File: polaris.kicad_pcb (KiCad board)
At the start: 4 copper layers, 75 x 155 mm, 163 parts, among them J1001 Conn_Coaxial, J101 XT60-M, J102 SPI, J103 I2C, J104 PB, J105 SWD, J106 PYRO5, J107 PYRO4, J108 PYRO3, J109 PYRO2, J110 PYRO1, J111 PYRO0, J112 SERVO0, J113 SERVO1, J114 SERVO2, J115 SERVO3, J116 SERVO4, J117 SERVO5, J301 USB_C_Receptacle_USB2.0_16P, J401 GNSS, J501 XT60-M, Q201 IRLZ44N, Q202 IRLZ44N, Q401 Q_NMOS, Q501 IRLZ44N, Q502 IRLZ44N, Q503 IRLZ44N, Q504 IRLZ44N, Q505 IRLZ44N, Q506 IRLZ44N, SW401 SW_Push, SW402 SW_Push, U1001 Ra-08H, U1101 THD-2528-11SD-GF, U1201 W25Q128JVE, U201 BQ24005, U202 LM74700, U203 LM74700, U204 TLV75733PDBV, U205 LMR51430, U206 TPS7A2033PDBVR, U301 USBLC6-2SC6, U302 CH224K, U303 USBLC6-2SC6, U401 STM32F446VETx, U501 PC817, U502 PC817, U503 CD4051B, U504 PC817, U505 PC817, U506 PC817, U507 PC817, U601 ICM-42688-P, U701 LSM6DSO32TR, U801 MS5607, U901 LPS22HH, Y401 YXC YSX321SL

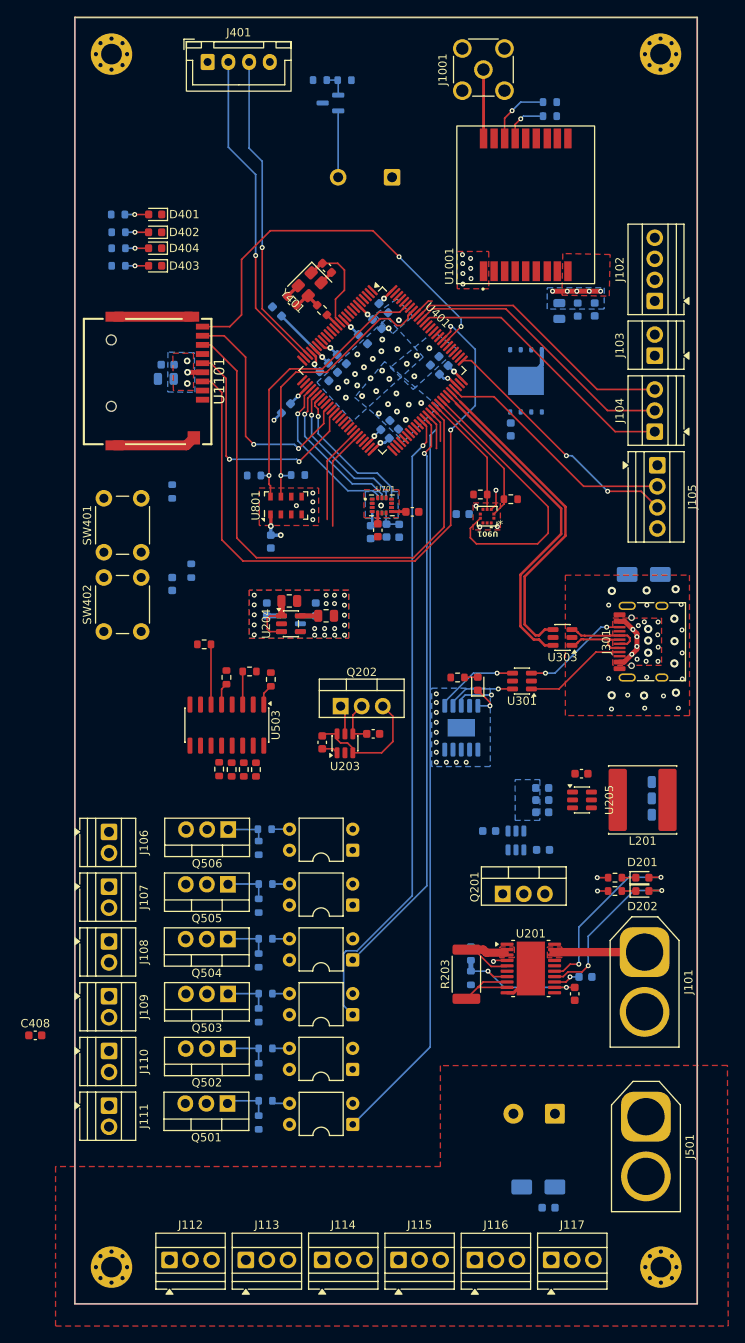
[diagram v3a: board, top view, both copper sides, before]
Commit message: Updated board to support any telemetry radio
Continued laying traces
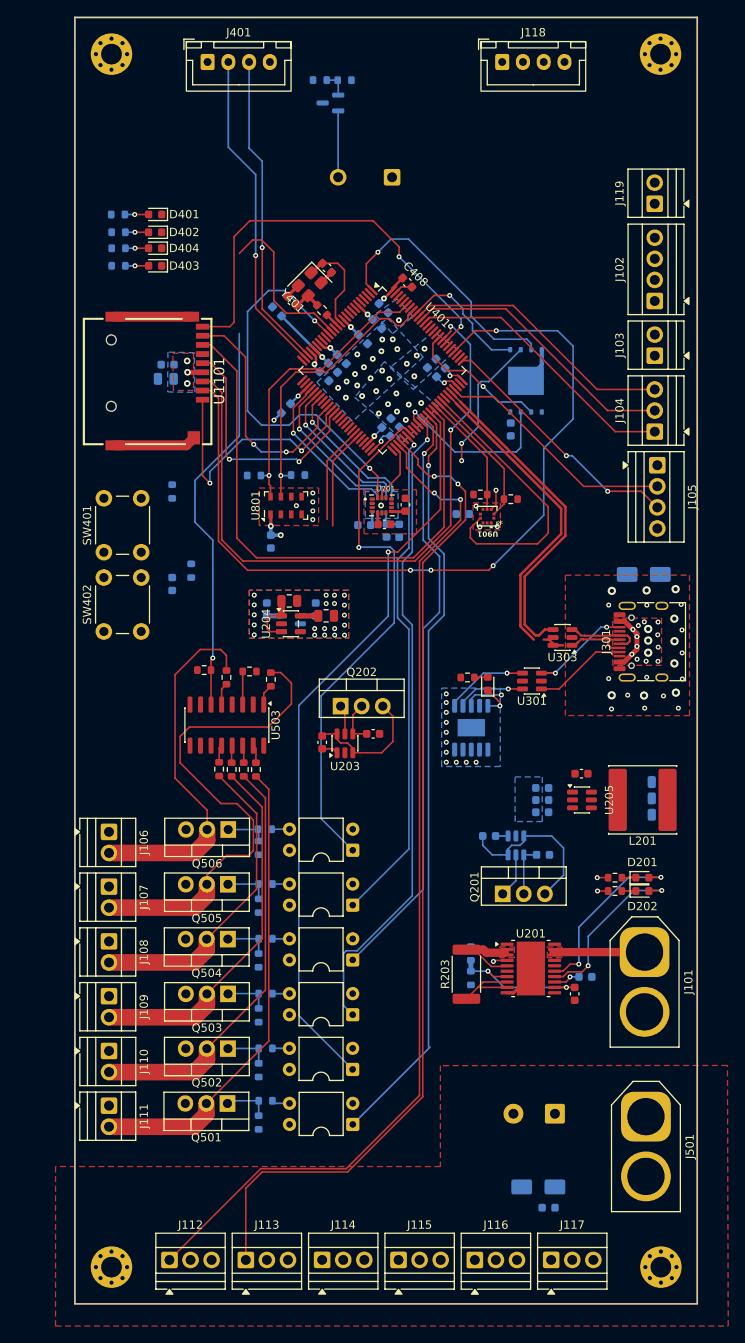
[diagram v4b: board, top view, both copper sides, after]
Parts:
- removed C1001: 47u, Capacitor_SMD:C_0805_2012Metric
- removed C1002: 100n, Capacitor_SMD:C_0603_1608Metric
- removed D1001: D_TVS, LED_SMD:LED_0603_1608Metric
- removed J1001: Conn_Coaxial, Connector_Coaxial:SMA_Molex_73251-2200_Horizontal
- removed R1001: 10k, Resistor_SMD:R_0603_1608Metric
- removed R1002: 810k, Resistor_SMD:R_0603_1608Metric
- removed U1001: Ra-08H, Polaris:RA-08H
- added J118: RADIO, Connector_JST:JST_XH_B4B-XH-A_1x04_P2.50mm_Vertical, F.Cu at (138.5, 30.4)
- added J119: POWER, TerminalBlock:TerminalBlock_Xinya_XY308-2.54-2P_1x02_P2.54mm_Horizontal, F.Cu at (156.9, 47.5)
- moved C408 101.2 mm to (127.1, 56.9), turned to -45 degrees
- moved R507 3.10 mm to (102.6, 103.6)
- moved D302 1.20 mm to (136.8, 105.3)
- moved R301 1.20 mm to (134.3, 104.5)
- moved U301 1.20 mm to (142.1, 105.0)
- moved U302 1.20 mm to (134.8, 110.6)
- moved C701 1.19 mm to (126.8, 83.7), turned to 90 degrees
- moved C602 1.15 mm to (121.9, 86.2), turned to 180 degrees
- moved C702 1.07 mm to (124.3, 86.1), turned to 0 degrees
- moved C205 0.60 mm to (143.4, 125.9)
- moved C203 0.60 mm to (136.9, 123.6)
- moved U202 0.60 mm to (140.2, 124.8)
- moved C407 0.47 mm to (130.0, 67.7)
- moved C413 0.47 mm to (131.1, 66.7)
- moved C406 0.27 mm to (124.5, 73.9)
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- renumbered R513 to R505, R505 to R513
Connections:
- R505 pad 1: /4_Pyrochannels/PYRO_2 -> /4_Pyrochannels/PYRO_0
- R505 pad 2: /4_Pyrochannels/PYRO_2 -> /4_Pyrochannels/PYRO_0
- R513 pad 1: /4_Pyrochannels/PYRO_0 -> /4_Pyrochannels/PYRO_2
- R513 pad 2: /4_Pyrochannels/PYRO_0 -> /4_Pyrochannels/PYRO_2
- U401 pad 38: /3_NavigationProcessor/RF_TX -> /3_NavigationProcessor/RF_RX
- U401 pad 39: /3_NavigationProcessor/RF_RX -> /3_NavigationProcessor/RF_TX
- U503 pad 13: /4_Pyrochannels/PYRO_0 -> /4_Pyrochannels/PYRO_2
- U503 pad 15: /4_Pyrochannels/PYRO_2 -> /4_Pyrochannels/PYRO_0
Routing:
- net /3_NavigationProcessor/SERVO_S0: track 0.00 -> 123.4 mm, vias 0 -> 2
- net /3_NavigationProcessor/SERVO_S1: track 0.00 -> 120.3 mm, vias 0 -> 2
- net /3_NavigationProcessor/SD_DAT3: track 0.00 -> 100.9 mm, vias 0 -> 4
- net /3_NavigationProcessor/PYRO_1: track 3.96 -> 90.1 mm, vias 0 -> 1
- net /3_NavigationProcessor/PYRO_5: track 0.00 -> 63.6 mm, vias 0 -> 1
- net /3_NavigationProcessor/PYRO_4: track 0.00 -> 61.1 mm, vias 0 -> 1
- net /4_Pyrochannels/PYRO_4: track 2.55 -> 63.2 mm
- net /3_NavigationProcessor/~{MUX_EN}: track 7.14 -> 67.7 mm, vias 0 -> 1
- net /4_Pyrochannels/PYRO_0: track 0.00 -> 59.0 mm
- net /4_Pyrochannels/PYRO_1: track 0.00 -> 52.6 mm
- net /3_NavigationProcessor/LSM_MOSI: track 0.00 -> 47.6 mm, vias 0 -> 2
- net /4_Pyrochannels/PYRO_2: track 0.00 -> 46.2 mm
- net /4_Pyrochannels/PYRO_5: track 2.69 -> 46.2 mm
- net /4_Pyrochannels/PYRO_3: track 0.00 -> 39.8 mm
- net /3_NavigationProcessor/FLASH_IO2: track 0.00 -> 31.6 mm, vias 0 -> 1
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- added copper zone on B.Cu, net POWER
- removed copper zone on B.Cu, net (none)
- removed copper zone on B.Cu, net +3.3VA
- removed copper zone on F.Cu, net +3.3VA
